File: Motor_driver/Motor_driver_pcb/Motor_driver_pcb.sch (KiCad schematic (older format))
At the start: 10 parts, among them J1 USB_B, U1 L7805, U2 FT232RL, U3 STM32F103C8T6, U4 CD40106BE, U5 CD40106BE, U6 CD40106BE, U7 CD40106BE

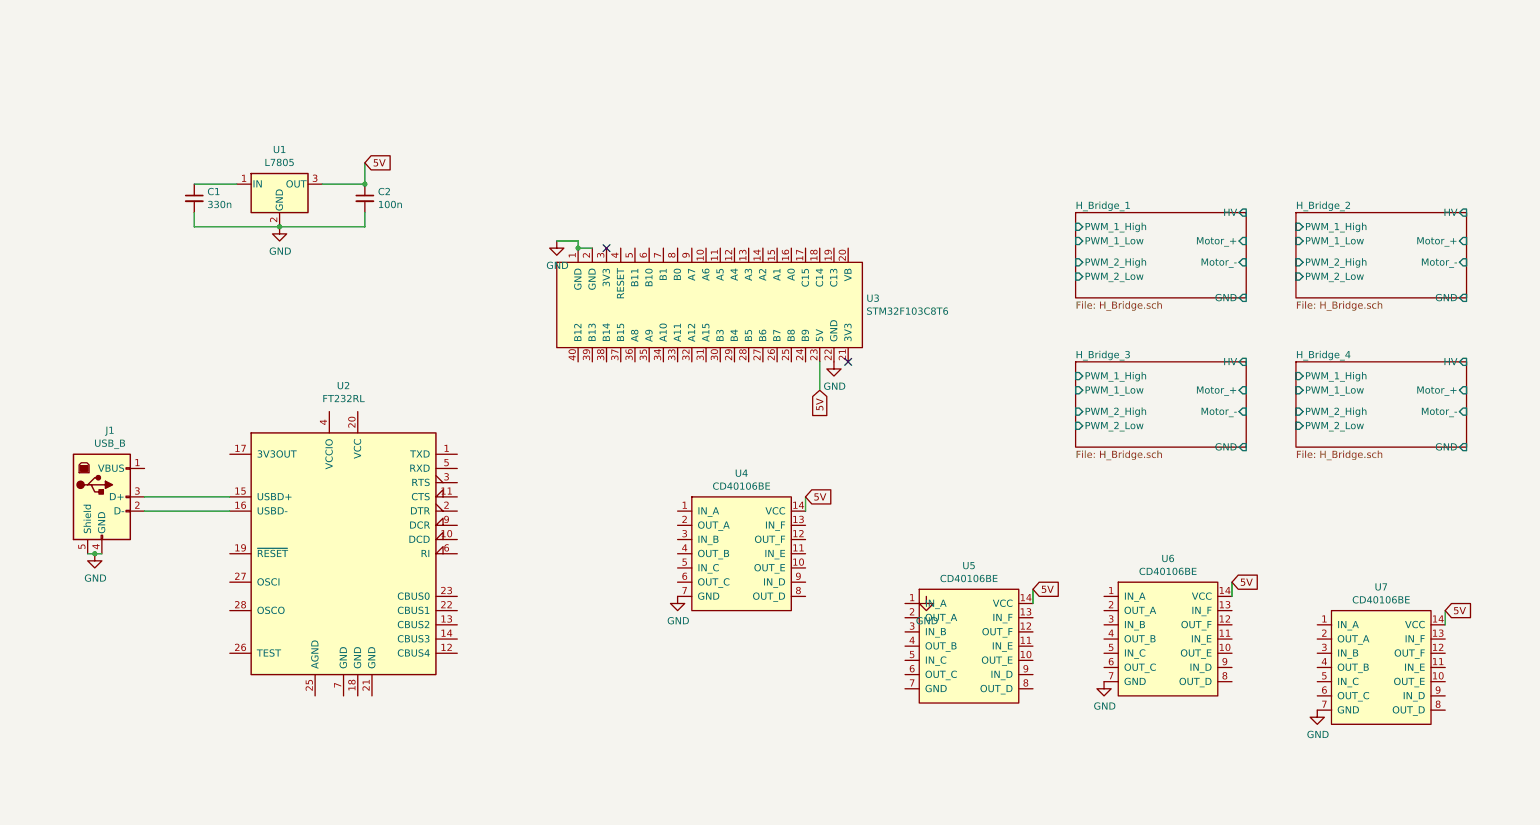
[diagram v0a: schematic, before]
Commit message: update driver schema add  uc config
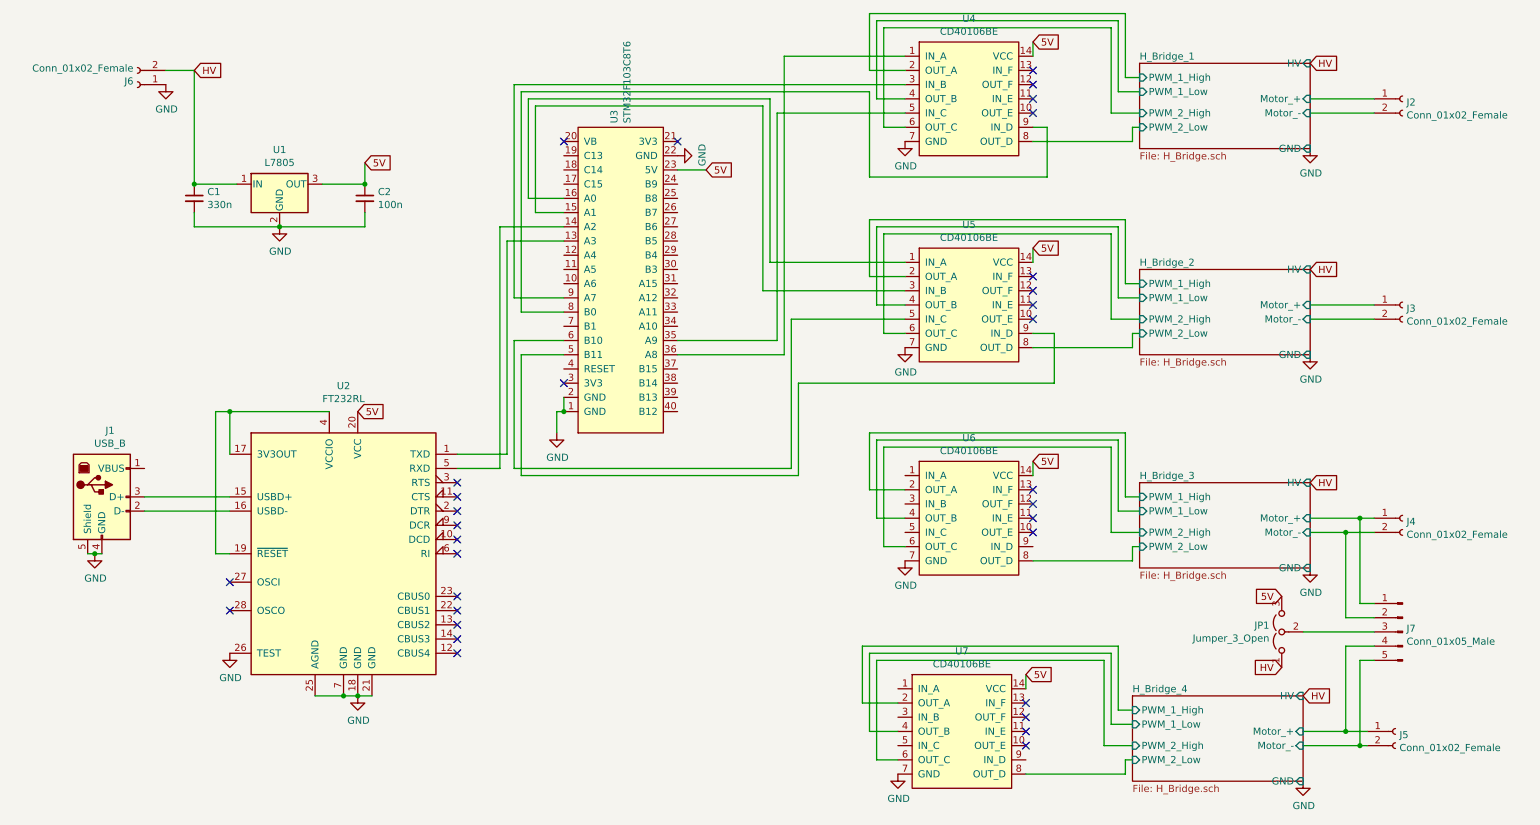
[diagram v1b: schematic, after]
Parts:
- added J2, J3, J4, J5, J6: Conn_01x02_Female, Connector_PinSocket_2.54mm:PinSocket_1x02_P2.54mm_Vertical, symbol Connector:Conn_01x02_Female
- added J7: Conn_01x05_Male, Connector_PinHeader_2.54mm:PinHeader_1x05_P2.54mm_Vertical, symbol Connector:Conn_01x05_Male
- added JP1: Jumper_3_Open, Connector_PinHeader_2.54mm:PinHeader_1x03_P2.54mm_Vertical, symbol Jumper:Jumper_3_Open
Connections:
- net 5V: now also U2.20 (VCC), JP1.3 (B)
- net GND: now also U2.18 (GND), U2.21 (GND), U2.25 (AGND), U2.26 (TEST), U2.7 (GND), U5.7 (GND), J6.1 (Pin_1)
- net H_Bridge_1/Motor_+: now also J2.1 (Pin_1)
- net H_Bridge_1/Motor_-: now also J2.2 (Pin_2)
- net H_Bridge_1/PWM_1_High: now also U4.2 (OUT_A)
- net H_Bridge_1/PWM_1_Low: now also U4.4 (OUT_B)
- net H_Bridge_1/PWM_2_High: now also U4.6 (OUT_C)
- net H_Bridge_1/PWM_2_Low: now also U4.8 (OUT_D)
- net H_Bridge_2/Motor_+: now also J3.1 (Pin_1)
- net H_Bridge_2/Motor_-: now also J3.2 (Pin_2)
- net H_Bridge_2/PWM_1_High: now also U5.2 (OUT_A)
- net H_Bridge_2/PWM_1_Low: now also U5.4 (OUT_B)
- net H_Bridge_2/PWM_2_High: now also U5.6 (OUT_C)
- net H_Bridge_2/PWM_2_Low: now also U5.8 (OUT_D)
- net H_Bridge_3/Motor_+: now also J4.1 (Pin_1), J7.1 (Pin_1)
- net H_Bridge_3/Motor_-: now also J4.2 (Pin_2), J7.2 (Pin_2)
- net H_Bridge_3/PWM_1_High: now also U6.2 (OUT_A)
- net H_Bridge_3/PWM_1_Low: now also U6.4 (OUT_B)
- net H_Bridge_3/PWM_2_High: now also U6.6 (OUT_C)
- net H_Bridge_3/PWM_2_Low: now also U6.8 (OUT_D)
- net H_Bridge_4/Motor_+: now also J5.1 (Pin_1), J7.4 (Pin_4)
- net H_Bridge_4/Motor_-: now also J5.2 (Pin_2), J7.5 (Pin_5)
- net H_Bridge_4/PWM_1_High: now also U7.2 (OUT_A)
- net H_Bridge_4/PWM_1_Low: now also U7.4 (OUT_B)
- net H_Bridge_4/PWM_2_High: now also U7.6 (OUT_C)
- net H_Bridge_4/PWM_2_Low: now also U7.8 (OUT_D)
- net at U3.13 (A3): now also U2.1 (TXD)
- net at U3.14 (A2): now also U2.5 (RXD)
- net at U3.15 (A1): now also U5.3 (IN_B)
- net at U3.16 (A0): now also U5.1 (IN_A)
- net at U3.35 (A9): now also U4.5 (IN_C)
- net at U3.36 (A8): now also U4.1 (IN_A)
- net at U3.5 (B11): now also U5.9 (IN_D)
- net at U3.6 (B10): now also U5.5 (IN_C)
- net at U3.8 (B0): now also U4.9 (IN_D)
- net at U3.9 (A7): now also U4.3 (IN_B)
- net HV: now reaches C1.1, U1.1 (IN)
- net HV: now also J6.2 (Pin_2), JP1.1 (A)
- net at U2.17 (3V3OUT): now also U2.19 (~RESET~), U2.4 (VCCIO)
- new net: J7.3 (Pin_3), JP1.2 (C)
- no-connect marks 2 -> 32
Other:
- moved on the sheet: U3, U4, U5, U6, U7

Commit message: update schema, create PCB
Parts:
- removed C1: 330n, symbol Device:C_Small
- removed C2: 100n, symbol Device:C_Small
- removed U1: L7805, Package_TO_SOT_THT:TO-220-3_Vertical, symbol Regulator_Linear:L7805
- removed U6, U7: CD40106BE, Package_DIP:DIP-14_W7.62mm, symbol My_Parts:CD40106BE
- added J3: Servo 1, Connector_PinHeader_2.54mm:PinHeader_1x03_P2.54mm_Vertical, symbol Connector:Conn_01x03_Male
- added J4: Servo 2, Connector_PinHeader_2.54mm:PinHeader_1x03_P2.54mm_Vertical, symbol Connector:Conn_01x03_Male
- added J5: Encoder 1, Connector_PinHeader_2.54mm:PinHeader_1x04_P2.54mm_Vertical, symbol Connector:Conn_01x04_Male
- added J6: Encoder 2, Connector_PinHeader_2.54mm:PinHeader_1x04_P2.54mm_Vertical, symbol Connector:Conn_01x04_Male
- added U1: LM2596S_Module, My_Footprints:LM2596_Module, symbol My_Parts:LM2596S_Module
- J10: renamed from J4; value Conn_01x02_Female -> Stepper AB; symbol Connector:Conn_01x02_Female -> Connector:Screw_Terminal_01x02
- J11: renamed from J7; value Conn_01x05_Male -> Uni_stepper
- J2: renamed from J6; value Conn_01x02_Female -> Power; symbol Connector:Conn_01x02_Female -> Connector:Screw_Terminal_01x02
- J7: renamed from J5; value Conn_01x02_Female -> Stepper CD; symbol Connector:Conn_01x02_Female -> Connector:Screw_Terminal_01x02
- J8: renamed from J2; value Conn_01x02_Female -> Motor 1; symbol Connector:Conn_01x02_Female -> Connector:Screw_Terminal_01x02
- J9: renamed from J3; value Conn_01x02_Female -> Motor 2; symbol Connector:Conn_01x02_Female -> Connector:Screw_Terminal_01x02
- JP1: value Jumper_3_Open -> Voltage switch
- renumbered U5 to U4, U4 to U5
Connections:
- net 5V: now also J3.2 (Pin_2), J4.2 (Pin_2), J5.4 (Pin_4), J6.4 (Pin_4), U1.3 (Out+); no longer U2.20 (VCC)
- net GND: now also J3.1 (Pin_1), J4.1 (Pin_1), J5.3 (Pin_3), J6.3 (Pin_3), U1.2 (In-), U1.4 (Out-)
- net HV: now also U1.1 (In+)
- net ENC1A: now reaches U3.10 (A6)
- net ENC1A: now also J5.1 (Pin_1)
- net at U3.15 (A1): now also J4.3 (Pin_3); no longer U4.3 (IN_B)
- net at U3.16 (A0): now also J3.3 (Pin_3); no longer U4.1 (IN_A)
- net ENC2B: now reaches U3.26 (B7)
- net ENC2B: now also J6.2 (Pin_2)
- net ENC2A: now reaches U3.27 (B6)
- net ENC2A: now also J6.1 (Pin_1)
- net at U3.33 (A11): now also U5.9 (IN_D)
- net at U3.34 (A10): now also U5.5 (IN_C)
- net at U3.35 (A9): now also U5.3 (IN_B); no longer U5.5 (IN_C)
- net at U3.37 (B15): now also U4.9 (IN_D)
- net at U3.38 (B14): now also U4.5 (IN_C)
- net at U3.39 (B13): now also U4.3 (IN_B)
- net at U3.40 (B12): now also U4.1 (IN_A)
- net at U3.5 (B11): no longer U4.9 (IN_D)
- net at U3.6 (B10): no longer U4.5 (IN_C)
- net at U3.8 (B0): no longer U5.9 (IN_D)
- net ENC1B: now reaches U3.9 (A7)
- net ENC1B: now also J5.2 (Pin_2); no longer U5.3 (IN_B)
- net at J1.1 (VBUS): now also U2.20 (VCC)
- net H_Bridge_1/PWM_1_High renamed H_Bridge_1/PWM_1
- net H_Bridge_1/PWM_1_Low renamed H_Bridge_1/PWM_2
- net H_Bridge_1/PWM_2_High renamed sheet5CA0C204/PWM_1
- net H_Bridge_1/PWM_2_Low renamed sheet5CA0C204/PWM_2
- net H_Bridge_2/Motor_+ renamed sheet5CA0C204/Motor_+
- net H_Bridge_2/Motor_- renamed sheet5CA0C204/Motor_-
- net H_Bridge_2/PWM_1_High renamed sheet5CA1B149/PWM_1
- net H_Bridge_2/PWM_1_Low renamed sheet5CA1B149/PWM_2
- net H_Bridge_2/PWM_2_High renamed sheet5CA227AD/PWM_1
- net H_Bridge_2/PWM_2_Low renamed sheet5CA227AD/PWM_2
- net H_Bridge_3/Motor_+ renamed sheet5CA1B149/Motor_+
- net H_Bridge_3/Motor_- renamed sheet5CA1B149/Motor_-
- net H_Bridge_4/Motor_+ renamed sheet5CA227AD/Motor_+
- net H_Bridge_4/Motor_- renamed sheet5CA227AD/Motor_-
- no-connect marks 32 -> 41
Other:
- moved on the sheet: J11, JP1, U4, U5

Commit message: finish schema and PCB update uC configuration
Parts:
- added C1: 10n, Capacitor_SMD:C_0805_2012Metric_Pad1.15x1.40mm_HandSolder, symbol Device:C_Small
- added C2: 4.7u, Capacitor_THT:CP_Radial_D5.0mm_P2.00mm, symbol Device:C_Small
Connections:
- net GND: now also J11.3 (Pin_3), C1.1, C2.1
- net at U3.13 (A3): no longer U2.1 (TXD)
- net at U3.14 (A2): no longer U2.5 (RXD)
- net SERVO1: now reaches J4.3 (Pin_3), U3.15 (A1)
- net SERVO2: now reaches J3.3 (Pin_3), U3.16 (A0)
- net at U3.5 (B11): now also U2.1 (TXD)
- net at U3.6 (B10): now also U2.5 (RXD)
- net at J1.1 (VBUS), U2.20 (VCC): now also C1.2, C2.2
- net sheet5CA1B149/HV: now reaches JP1.2 (C)
- net sheet5CA1B149/HV: no longer J11.3 (Pin_3)
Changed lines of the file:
@@
 Text GLabel 8900 1950 2    50   Input ~ 0
 HV
-Text GLabel 8900 3150 2    50   Input ~ 0
-HV
-Text GLabel 8850 4650 2    50   Input ~ 0
-HV
 Wire Wire Line
 	2800 3350 2100 3350
 Wire Wire Line
 	2100 3350 2100 3650
-Wire Wire Line
-	3900 2050 3900 3750
-Wire Wire Line
-	3950 2150 3950 3650
 NoConn ~ 4450 1450
-$Comp
-L power:GND #PWR03
-U 1 1 5CA960B0
-P 2100 5050
-F 0 "#PWR03" H 2100 4800 50  0001 C CNN
-F 1 "GND" H 2105 4877 50  0000 C CNN
-F 2 "" H 2100 5050 50  0001 C CNN
-F 3 "" H 2100 5050 50  0001 C CNN
-	1    2100 5050
-	1    0    0    -1
-$EndComp
 NoConn ~ 2100 4550
 NoConn ~ 2100 4750
@@
 	2000 3350 2100 3350
 Connection ~ 2100 3350
-Connection ~ 3000 5350
-Wire Wire Line
-	3000 5350 3100 5350
-$Comp
-L power:GND #PWR05
-U 1 1 5CACBE84
-P 3000 5350
-F 0 "#PWR05" H 3000 5100 50  0001 C CNN
-F 1 "GND" H 3005 5177 50  0000 C CNN
-F 2 "" H 3000 5350 50  0001 C CNN
-F 3 "" H 3000 5350 50  0001 C CNN
-	1    3000 5350
-	1    0    0    -1
-$EndComp
 $Comp
 L Connector:Conn_01x05_Male J11
@@
 	0    -1   -1   0
 $EndComp
-Wire Wire Line
-	8850 4200 9350 4200
 Text GLabel 8700 3950 0    50   Input ~ 0
 5V
@@
 NoConn ~ 4450 2650
 NoConn ~ 4450 2750
-NoConn ~ 4450 2850
-NoConn ~ 4450 2950
 NoConn ~ 4450 3050
 $Comp
@@
 ENC2B
 Wire Wire Line
-	3900 3750 3700 3750
-Wire Wire Line
-	3950 3650 3700 3650
-Wire Wire Line
 	4000 1850 4000 5450
 Wire Wire Line
@@
 Wire Wire Line
 	4000 1850 4450 1850
-Wire Wire Line
-	3900 2050 4450 2050
-Wire Wire Line
-	3950 2150 4450 2150
 Wire Wire Line
 	4050 1950 4450 1950
@@
 	1700 950  1800 950
 Wire Wire Line
-	2900 5350 3000 5350
-Wire Wire Line
-	2700 5350 2900 5350
-Connection ~ 2900 5350
+	1500 3750 1600 3750
+Wire Wire Line
+	1950 3750 1950 3300
+Wire Wire Line
+	1950 3300 3000 3300
+Wire Wire Line
+	3000 3300 3000 3350
+$Comp
+L My_Parts:LM2596S_Module U1
+U 1 1 5CC2DAE3
+P 2700 1600
+F 0 "U1" H 2700 2025 50  0000 C CNN
+F 1 "LM2596S_Module" H 2700 1934 50  0000 C CNN
+F 2 "My_Footprints:LM2596_Module" H 2700 1600 50  0001 C CNN
+F 3 "" H 2700 1600 50  0001 C CNN
+	1    2700 1600
+	1    0    0    -1
+$EndComp
+$Comp
+L power:GND #PWR06
+U 1 1 5CC466AB
+P 3150 1800
+F 0 "#PWR06" H 3150 1550 50  0001 C CNN
+F 1 "GND" H 3155 1627 50  0000 C CNN
+F 2 "" H 3150 1800 50  0001 C CNN
+F 3 "" H 3150 1800 50  0001 C CNN
+	1    3150 1800
+	1    0    0    -1
+$EndComp
+$Comp
+L power:GND #PWR04
+U 1 1 5CC470D9
+P 2250 1800
+F 0 "#PWR04" H 2250 1550 50  0001 C CNN
+F 1 "GND" H 2255 1627 50  0000 C CNN
+F 2 "" H 2250 1800 50  0001 C CNN
+F 3 "" H 2250 1800 50  0001 C CNN
+	1    2250 1800
+	1    0    0    -1
+$EndComp
+Wire Wire Line
+	1800 950  1800 1400
+Wire Wire Line
+	1800 1400 2250 1400
+Connection ~ 1800 950
+Wire Wire Line
+	1800 950  1850 950
+Wire Wire Line
+	3600 1400 3150 1400
+$Comp
+L power:GND #PWR0101
+U 1 1 5CA89C28
+P 9350 4200
+F 0 "#PWR0101" H 9350 3950 50  0001 C CNN
+F 1 "GND" V 9355 4072 50  0000 R CNN
+F 2 "" H 9350 4200 50  0001 C CNN
+F 3 "" H 9350 4200 50  0001 C CNN
+	1    9350 4200
+	0    1    1    0
+$EndComp
+Wire Wire Line
+	8850 4200 9050 4200
+Wire Wire Line
+	9050 3150 8900 3150
+Wire Wire Line
+	9050 3150 9050 4200
+Wire Wire Line
+	9050 4200 9050 4650
+Wire Wire Line
+	9050 4650 8850 4650
+Connection ~ 9050 4200
 $Comp
 L Interface_USB:FT232RL U2
@@
 $EndComp
 Wire Wire Line
-	1500 3750 1950 3750
-Wire Wire Line
-	1950 3750 1950 3300
-Wire Wire Line
-	1950 3300 3000 3300
-Wire Wire Line
-	3000 3300 3000 3350
-$Comp
-L My_Parts:LM2596S_Module U1
-U 1 1 5CC2DAE3
-P 2700 1600
-F 0 "U1" H 2700 2025 50  0000 C CNN
-F 1 "LM2596S_Module" H 2700 1934 50  0000 C CNN
-F 2 "My_Footprints:LM2596_Module" H 2700 1600 50  0001 C CNN
-F 3 "" H 2700 1600 50  0001 C CNN
-	1    2700 1600
-	1    0    0    -1
-$EndComp
-$Comp
-L power:GND #PWR06
-U 1 1 5CC466AB
-P 3150 1800
-F 0 "#PWR06" H 3150 1550 50  0001 C CNN
-F 1 "GND" H 3155 1627 50  0000 C CNN
-F 2 "" H 3150 1800 50  0001 C CNN
-F 3 "" H 3150 1800 50  0001 C CNN
-	1    3150 1800
-	1    0    0    -1
-$EndComp
-$Comp
-L power:GND #PWR04
-U 1 1 5CC470D9
-P 2250 1800
-F 0 "#PWR04" H 2250 1550 50  0001 C CNN
-F 1 "GND" H 2255 1627 50  0000 C CNN
-F 2 "" H 2250 1800 50  0001 C CNN
-F 3 "" H 2250 1800 50  0001 C CNN
-	1    2250 1800
-	1    0    0    -1
-$EndComp
-Wire Wire Line
-	1800 950  1800 1400
-Wire Wire Line
-	1800 1400 2250 1400
-Connection ~ 1800 950
-Wire Wire Line
-	1800 950  1850 950
-Wire Wire Line
-	3600 1400 3150 1400
+	2100 5050 2100 5350
+Wire Wire Line
+	2100 5350 2700 5350
+Connection ~ 2700 5350
+Wire Wire Line
+	2700 5350 2900 5350
+Connection ~ 2900 5350
+Wire Wire Line
+	2900 5350 3000 5350
+Connection ~ 3000 5350
+Wire Wire Line
+	3000 5350 3100 5350
+$Comp
+L power:GND #PWR0102
+U 1 1 5CAB0288
+P 2100 5350
+F 0 "#PWR0102" H 2100 5100 50  0001 C CNN
+F 1 "GND" H 2105 5177 50  0000 C CNN
+F 2 "" H 2100 5350 50  0001 C CNN
+F 3 "" H 2100 5350 50  0001 C CNN
+	1    2100 5350
+	1    0    0    -1
+$EndComp
+Connection ~ 2100 5350
+Text GLabel 4800 4450 2    50   Input ~ 0
+SERVO1
+Text GLabel 4000 4750 2    50   Input ~ 0
+SERVO2
+NoConn ~ 4450 2050
+NoConn ~ 4450 2150
+Wire Wire Line
+	4450 2850 4200 2850
+Wire Wire Line
+	4200 2850 4200 3750
+Wire Wire Line
+	4200 3750 3700 3750
+Wire Wire Line
+	3700 3650 4150 3650
+Wire Wire Line
+	4150 3650 4150 2950
+Wire Wire Line
+	4150 2950 4450 2950
+$Comp
+L Device:C_Small C1
+U 1 1 5CAD538D
+P 1600 3650
+F 0 "C1" H 1692 3696 50  0000 L CNN
+F 1 "10n" H 1692 3605 50  0000 L CNN
+F 2 "Capacitor_SMD:C_0805_2012Metric_Pad1.15x1.40mm_HandSolder" H 1600 3650 50  0001 C CNN
+F 3 "~" H 1600 3650 50  0001 C CNN
+	1    1600 3650
+	1    0    0    -1
+$EndComp
+Connection ~ 1600 3750
+Wire Wire Line
+	1600 3750 1850 3750
+$Comp
+L power:GND #PWR0103
+U 1 1 5CAD5A18
+P 1600 3550
+F 0 "#PWR0103" H 1600 3300 50  0001 C CNN
+F 1 "GND" H 1605 3377 50  0000 C CNN
+F 2 "" H 1600 3550 50  0001 C CNN
+F 3 "" H 1600 3550 50  0001 C CNN
+	1    1600 3550
+	-1   0    0    1
+$EndComp
+$Comp
+L Device:C_Small C2
+U 1 1 5CAD6164
+P 1850 3650
+F 0 "C2" H 1942 3696 50  0000 L CNN
+F 1 "4.7u" H 1942 3605 50  0000 L CNN
+F 2 "Capacitor_THT:CP_Radial_D5.0mm_P2.00mm" H 1850 3650 50  0001 C CNN
+F 3 "~" H 1850 3650 50  0001 C CNN
+	1    1850 3650
+	1    0    0    -1
+$EndComp
+Connection ~ 1850 3750
+Wire Wire Line
+	1850 3750 1950 3750
+$Comp
+L power:GND #PWR0104
+U 1 1 5CAD6A26
+P 1850 3550
+F 0 "#PWR0104" H 1850 3300 50  0001 C CNN
+F 1 "GND" H 1855 3377 50  0000 C CNN
+F 2 "" H 1850 3550 50  0001 C CNN
+F 3 "" H 1850 3550 50  0001 C CNN
+	1    1850 3550
+	-1   0    0    1
+$EndComp
 $EndSCHEMATC

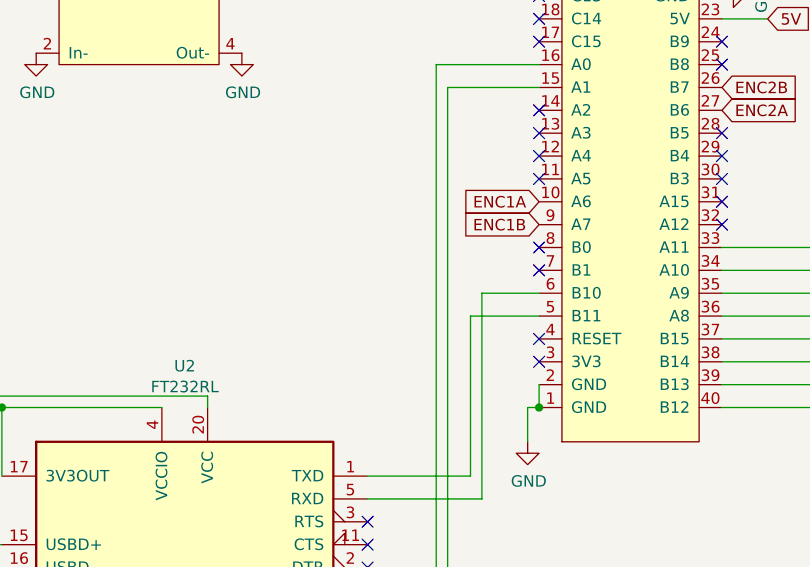
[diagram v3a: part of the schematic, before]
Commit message: add BT_module PCB add Gerbera files
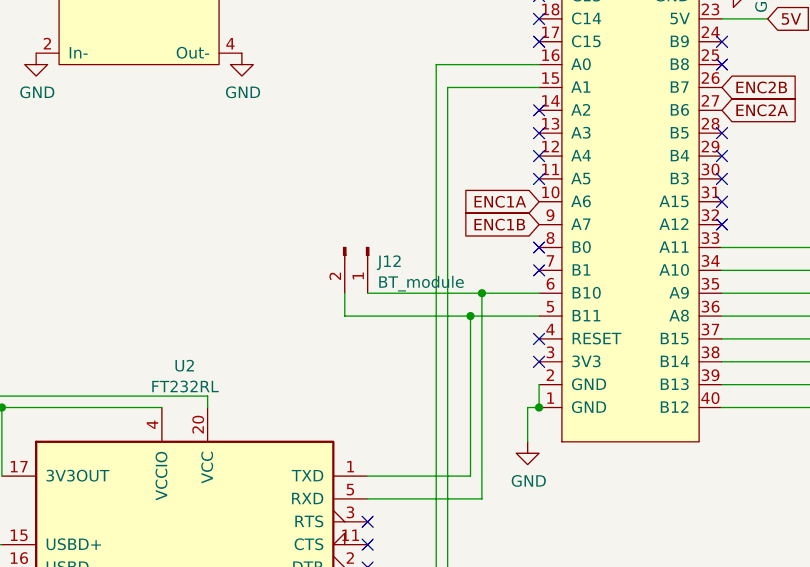
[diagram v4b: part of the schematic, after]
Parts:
- added J12: BT_module, Connector_PinHeader_2.54mm:PinHeader_1x02_P2.54mm_Vertical, symbol Connector:Conn_01x02_Male
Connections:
- net at U2.1 (TXD), U3.5 (B11): now also J12.2 (Pin_2)
- net at U2.5 (RXD), U3.6 (B10): now also J12.1 (Pin_1)
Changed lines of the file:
@@
 	-1   0    0    1
 $EndComp
+$Comp
+L Connector:Conn_01x02_Male J12
+U 1 1 5CAF16CC
+P 3700 2650
+F 0 "J12" V 3762 2694 50  0000 L CNN
+F 1 "BT_module" V 3853 2694 50  0000 L CNN
+F 2 "Connector_PinHeader_2.54mm:PinHeader_1x02_P2.54mm_Vertical" H 3700 2650 50  0001 C CNN
+F 3 "~" H 3700 2650 50  0001 C CNN
+	1    3700 2650
+	0    1    1    0
+$EndComp
+Wire Wire Line
+	4200 2850 3700 2850
+Connection ~ 4200 2850
+Wire Wire Line
+	3600 2850 3600 2950
+Wire Wire Line
+	3600 2950 4150 2950
+Connection ~ 4150 2950
 $EndSCHEMATC
